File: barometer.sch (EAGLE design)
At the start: 91 parts, among them IC1 MIC5225-3.3v, IC2 TPS5410, IC3 ZPA2326-0311A-R, U1 MCP4725, U2 LTC2850, U3 PCA9306, U4 MAX3221, U5 XC6215XC6215B182NR, U6 Tiny85-20-SMT, X2 1751264, X3 1751248

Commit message: Migrate to customised/forked libraries
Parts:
- SJ1, SJ10, SJ11, SJ12, SJ2, SJ3, SJ4, SJ5, SJ6, SJ7, SJ8, SJ9: device SparkFun-Retired:SOLDERJUMPERTRACE -> SparkFun-Retired-0:SOLDERJUMPERTRACE
- U3: device SparkFun-IC-Comms:PCA9306 -> v-shifter-sparkfun:PCA9306
- U6: device SparkFun-Retired:ATTINY45TINY85-20-SMT -> SparkFun-Retired-0:ATTINY45TINY85-20-SMT
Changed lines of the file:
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@@
 <part name="TP4" library="testpad" library_urn="urn:adsk.eagle:library:385" deviceset="PTR1" device="B1,27" package3d_urn="urn:adsk.eagle:package:27944/1"/>
 <part name="TP5" library="testpad" library_urn="urn:adsk.eagle:library:385" deviceset="PTR1" device="B1,27" package3d_urn="urn:adsk.eagle:package:27944/1"/>
-<part name="SJ1" library="SparkFun-Retired" deviceset="SOLDERJUMPER" device="TRACE"/>
-<part name="SJ2" library="SparkFun-Retired" deviceset="SOLDERJUMPER" device="TRACE"/>
-<part name="SJ3" library="SparkFun-Retired" deviceset="SOLDERJUMPER" device="TRACE"/>
-<part name="SJ4" library="SparkFun-Retired" deviceset="SOLDERJUMPER" device="TRACE"/>
+<part name="SJ1" library="SparkFun-Retired-0" deviceset="SOLDERJUMPER" device="TRACE"/>
+<part name="SJ2" library="SparkFun-Retired-0" deviceset="SOLDERJUMPER" device="TRACE"/>
+<part name="SJ3" library="SparkFun-Retired-0" deviceset="SOLDERJUMPER" device="TRACE"/>
+<part name="SJ4" library="SparkFun-Retired-0" deviceset="SOLDERJUMPER" device="TRACE"/>
 <part name="U$1" library="microbuilder" deviceset="MOUNTINGHOLE" device="2.5"/>
 <part name="U$2" library="microbuilder" deviceset="MOUNTINGHOLE" device="2.5"/>
@@
 <part name="TP13" library="testpad" library_urn="urn:adsk.eagle:library:385" deviceset="PTR1" device="B1,27" package3d_urn="urn:adsk.eagle:package:27944/1"/>
 <part name="TP14" library="testpad" library_urn="urn:adsk.eagle:library:385" deviceset="PTR1" device="B1,27" package3d_urn="urn:adsk.eagle:package:27944/1"/>
-<part name="U6" library="SparkFun-Retired" deviceset="ATTINY45" device="TINY85-20-SMT" value="Tiny85-20-SMT"/>
-<part name="SJ5" library="SparkFun-Retired" deviceset="SOLDERJUMPER" device="TRACE"/>
-<part name="SJ6" library="SparkFun-Retired" deviceset="SOLDERJUMPER" device="TRACE"/>
-<part name="SJ7" library="SparkFun-Retired" deviceset="SOLDERJUMPER" device="TRACE"/>
-<part name="SJ8" library="SparkFun-Retired" deviceset="SOLDERJUMPER" device="TRACE"/>
-<part name="SJ9" library="SparkFun-Retired" deviceset="SOLDERJUMPER" device="TRACE"/>
+<part name="U6" library="SparkFun-Retired-0" deviceset="ATTINY45" device="TINY85-20-SMT" value="Tiny85-20-SMT"/>
+<part name="SJ5" library="SparkFun-Retired-0" deviceset="SOLDERJUMPER" device="TRACE"/>
+<part name="SJ6" library="SparkFun-Retired-0" deviceset="SOLDERJUMPER" device="TRACE"/>
+<part name="SJ7" library="SparkFun-Retired-0" deviceset="SOLDERJUMPER" device="TRACE"/>
+<part name="SJ8" library="SparkFun-Retired-0" deviceset="SOLDERJUMPER" device="TRACE"/>
+<part name="SJ9" library="SparkFun-Retired-0" deviceset="SOLDERJUMPER" device="TRACE"/>
 <part name="U1" library="microbuilder" deviceset="DAC_MCP4725" device="" value="MCP4725"/>
 <part name="X3" library="con-phoenix-350" library_urn="urn:adsk.eagle:library:174" deviceset="1751248" device="" package3d_urn="urn:adsk.eagle:package:9395/1"/>
 <part name="X2" library="con-phoenix-350" library_urn="urn:adsk.eagle:library:174" deviceset="1751264" device="" package3d_urn="urn:adsk.eagle:package:9397/1"/>
-<part name="U3" library="SparkFun-IC-Comms" deviceset="PCA9306" device="" value="PCA9306"/>
-<part name="SJ10" library="SparkFun-Retired" deviceset="SOLDERJUMPER" device="TRACE"/>
-<part name="SJ11" library="SparkFun-Retired" deviceset="SOLDERJUMPER" device="TRACE"/>
+<part name="U3" library="v-shifter-sparkfun" deviceset="PCA9306" device="" value="PCA9306"/>
+<part name="SJ10" library="SparkFun-Retired-0" deviceset="SOLDERJUMPER" device="TRACE"/>
+<part name="SJ11" library="SparkFun-Retired-0" deviceset="SOLDERJUMPER" device="TRACE"/>
 <part name="TP15" library="testpad" library_urn="urn:adsk.eagle:library:385" deviceset="PTR1" device="B1,27" package3d_urn="urn:adsk.eagle:package:27944/1"/>
 <part name="TP16" library="testpad" library_urn="urn:adsk.eagle:library:385" deviceset="PTR1" device="B1,27" package3d_urn="urn:adsk.eagle:package:27944/1"/>
@@
 <part name="C15" library="microbuilder" deviceset="CAP_CERAMIC" device="1206" value="47u"/>
 <part name="TP17" library="testpad" library_urn="urn:adsk.eagle:library:385" deviceset="PTR1" device="B1,27" package3d_urn="urn:adsk.eagle:package:27944/1"/>
-<part name="SJ12" library="SparkFun-Retired" deviceset="SOLDERJUMPER" device="TRACE"/>
+<part name="SJ12" library="SparkFun-Retired-0" deviceset="SOLDERJUMPER" device="TRACE"/>
 <part name="JP1" library="microbuilder" deviceset="HEADER-1X3" device="SMT" value="Analog Output Format"/>
 <part name="JP2" library="microbuilder" deviceset="HEADER-1X3" device="SMT" value="Digital Output Format"/>

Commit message: Update all libraries
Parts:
- D2: value B340A -> 3A/40V/500mV
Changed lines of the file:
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@@
 </classes>
 <parts>
-<part name="IC1" library="adafruit" deviceset="LP298X" device="S" value="MIC5225-3.3v"/>
-<part name="D1" library="adafruit" deviceset="DIODE" device="_SOD-123FL" value="SCHOTTKY"/>
+<part name="IC1" library="adafruit" library_urn="urn:adsk.eagle:library:420" deviceset="LP298X" device="S" value="MIC5225-3.3v"/>
+<part name="D1" library="adafruit" library_urn="urn:adsk.eagle:library:420" deviceset="DIODE" device="_SOD-123FL" value="SCHOTTKY"/>
 <part name="U4" library="texas-msp" deviceset="MAX3221" device="-TSSOP16" value="MAX3221"/>
 <part name="FRAME4" library="microbuilder" deviceset="FRAME_A4" device=""/>
@@
 <part name="C8" library="microbuilder" deviceset="CAP_CERAMIC" device="0603" value="4.7u"/>
 <part name="C9" library="microbuilder" deviceset="CAP_CERAMIC" device="0603" value="0.01u"/>
-<part name="D2" library="SparkFun-DiscreteSemi" deviceset="DIODE-SCHOTTKY" device="-B340A" value="B340A"/>
+<part name="D2" library="SparkFun-DiscreteSemi" library_urn="urn:adsk.eagle:library:514" deviceset="DIODE-SCHOTTKY" device="-B340A" package3d_urn="urn:adsk.eagle:package:38443/1" value="3A/40V/500mV"/>
 <part name="L1" library="Particle" deviceset="INDUCTOR-SPARKFUN" device="1210" value="68u"/>
 <part name="R20" library="microbuilder" deviceset="RESISTOR" device="0603" value="10k"/>

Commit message: Fix inductor's footprint's dimensions
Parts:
- L1: device Particle:INDUCTOR-SPARKFUN1210 -> inductor-tdk:INDUCTOR-TDKVLS6045EX
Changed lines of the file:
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@@
 <part name="C9" library="microbuilder" deviceset="CAP_CERAMIC" device="0603" value="0.01u"/>
 <part name="D2" library="SparkFun-DiscreteSemi" library_urn="urn:adsk.eagle:library:514" deviceset="DIODE-SCHOTTKY" device="-B340A" package3d_urn="urn:adsk.eagle:package:38443/1" value="3A/40V/500mV"/>
-<part name="L1" library="Particle" deviceset="INDUCTOR-SPARKFUN" device="1210" value="68u"/>
+<part name="L1" library="inductor-tdk" deviceset="INDUCTOR-TDK" device="VLS6045EX" value="68u"/>
 <part name="R20" library="microbuilder" deviceset="RESISTOR" device="0603" value="10k"/>
 <part name="R21" library="microbuilder" deviceset="RESISTOR" device="0603" value="3.24k"/>

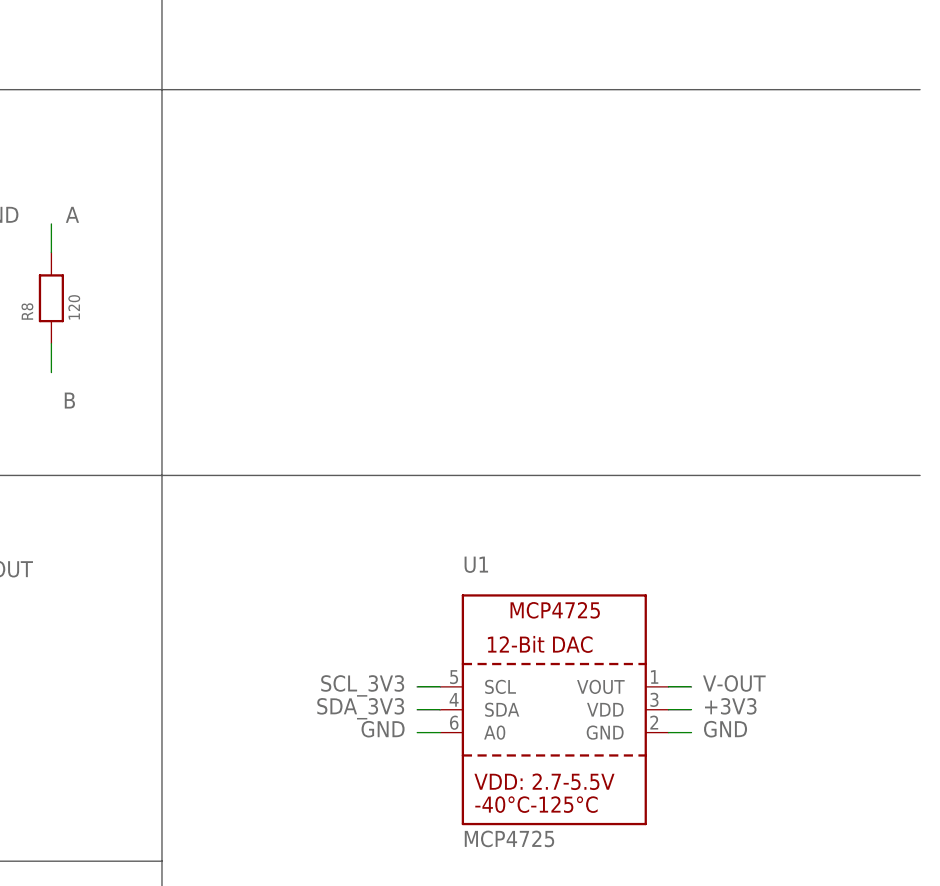
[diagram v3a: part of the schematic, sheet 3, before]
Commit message: Fix DAC output's voltage reference from +3V3 to +5V0
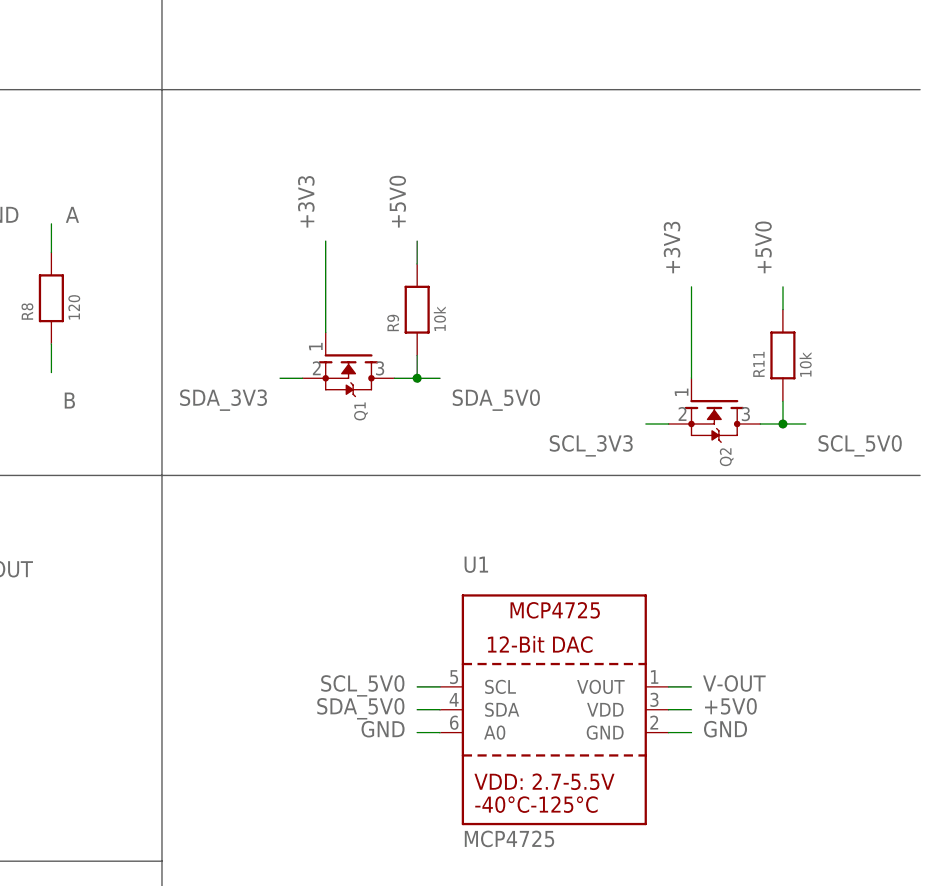
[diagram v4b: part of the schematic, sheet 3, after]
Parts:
- added Q1, Q2: (no value), microbuilder:MOSFET-NWIDE
- added R11, R9: 10k, microbuilder:RESISTOR0603
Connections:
- new net SCL_5V0: Q2.D, R11.1, U1.SCL
- new net SDA_5V0: Q1.D, R9.1, U1.SDA
- net +3V3: now also Q1.G, Q2.G; no longer U1.VDD
- net +5V0: now also R11.2, R9.2, U1.VDD
- net SCL_3V3: now also Q2.S; no longer U1.SCL
- net SDA_3V3: now also Q1.S; no longer U1.SDA
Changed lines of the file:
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@@
 <classes>
 <class number="0" name="default" width="0" drill="0">
-<clearance class="0" value="0.205"/>
 </class>
 <class number="1" name="power" width="0.3048" drill="0">
@@
 <part name="PAD2" library="wirepad" library_urn="urn:adsk.eagle:library:412" deviceset="SMD2" device="" package3d_urn="urn:adsk.eagle:package:30839/1"/>
 <part name="PAD3" library="wirepad" library_urn="urn:adsk.eagle:library:412" deviceset="SMD2" device="" package3d_urn="urn:adsk.eagle:package:30839/1"/>
+<part name="R9" library="microbuilder" deviceset="RESISTOR" device="0603" value="10k"/>
+<part name="R11" library="microbuilder" deviceset="RESISTOR" device="0603" value="10k"/>
+<part name="Q1" library="microbuilder" deviceset="MOSFET-N" device="WIDE"/>
+<part name="Q2" library="microbuilder" deviceset="MOSFET-N" device="WIDE"/>
 </parts>
 <sheets>
@@
 <instance part="JP1" gate="A" x="46.99" y="35.56"/>
 <instance part="JP2" gate="A" x="46.99" y="15.24"/>
+<instance part="R9" gate="G$1" x="200.66" y="107.95" rot="R90"/>
+<instance part="R11" gate="G$1" x="241.3" y="102.87" rot="R90"/>
+<instance part="Q1" gate="G$1" x="193.04" y="102.87" rot="R270"/>
+<instance part="Q2" gate="G$1" x="233.68" y="97.79" rot="R270"/>
 </instances>
 <busses>
@@
 </segment>
 <segment>
-<pinref part="U1" gate="G$1" pin="VDD"/>
-<wire x1="228.6" y1="63.5" x2="231.14" y2="63.5" width="0.1524" layer="91"/>
-<label x="232.41" y="64.77" size="1.778" layer="95" rot="MR180"/>
+<wire x1="190.5" y1="105.41" x2="190.5" y2="115.57" width="0.1524" layer="91"/>
+<pinref part="Q1" gate="G$1" pin="G"/>
+<label x="189.23" y="116.84" size="1.778" layer="95" font="vector" rot="R90"/>
+</segment>
+<segment>
+<wire x1="231.14" y1="100.33" x2="231.14" y2="110.49" width="0.1524" layer="91"/>
+<pinref part="Q2" gate="G$1" pin="G"/>
+<label x="229.87" y="111.76" size="1.778" layer="95" font="vector" rot="R90"/>
 </segment>
 </net>
@@
 <net name="SDA_3V3" class="0">
 <segment>
+<wire x1="187.96" y1="100.33" x2="185.42" y2="100.33" width="0.1524" layer="91"/>
+<label x="184.15" y="99.06" size="1.778" layer="95" font="vector" rot="R180"/>
+<pinref part="Q1" gate="G$1" pin="S"/>
+</segment>
+</net>
+<net name="SCL_3V3" class="0">
+<segment>
+<wire x1="228.6" y1="95.25" x2="226.06" y2="95.25" width="0.1524" layer="91"/>
+<label x="224.79" y="93.98" size="1.778" layer="95" font="vector" rot="R180"/>
+<pinref part="Q2" gate="G$1" pin="S"/>
+</segment>
+</net>
+<net name="A-OUT" class="0">
+<segment>
+<wire x1="123.19" y1="13.97" x2="125.73" y2="13.97" width="0.1524" layer="91"/>
+<label x="127" y="15.24" size="1.778" layer="95"/>
+<pinref part="X2" gate="-3" pin="K"/>
+</segment>
+<segment>
+<wire x1="44.45" y1="35.56" x2="38.1" y2="35.56" width="0.1524" layer="91"/>
+<label x="36.83" y="36.83" size="1.778" layer="95" font="vector" rot="R180"/>
+<pinref part="JP1" gate="A" pin="2"/>
+</segment>
+</net>
+<net name="V-OUT" class="0">
+<segment>
+<pinref part="U1" gate="G$1" pin="VOUT"/>
+<wire x1="228.6" y1="66.04" x2="231.14" y2="66.04" width="0.1524" layer="91"/>
+<label x="232.41" y="67.31" size="1.778" layer="95" rot="MR180"/>
+</segment>
+<segment>
+<wire x1="44.45" y1="38.1" x2="38.1" y2="38.1" width="0.1524" layer="91"/>
+<label x="36.83" y="39.37" size="1.778" layer="95" font="vector" rot="R180"/>
+<pinref part="JP1" gate="A" pin="1"/>
+</segment>
+<segment>
+<pinref part="TP15" gate="G$1" pin="TP"/>
+<wire x1="50.8" y1="154.94" x2="50.8" y2="157.48" width="0.1524" layer="91"/>
+<label x="52.07" y="158.75" size="1.778" layer="95" rot="R90"/>
+</segment>
+</net>
+<net name="I-OUT" class="0">
+<segment>
+<wire x1="44.45" y1="33.02" x2="38.1" y2="33.02" width="0.1524" layer="91"/>
+<label x="36.83" y="34.29" size="1.778" layer="95" font="vector" rot="R180"/>
+<pinref part="JP1" gate="A" pin="3"/>
+</segment>
+<segment>
+<pinref part="TP16" gate="G$1" pin="TP"/>
+<wire x1="55.88" y1="154.94" x2="55.88" y2="157.48" width="0.1524" layer="91"/>
+<label x="57.15" y="158.75" size="1.778" layer="95" rot="R90"/>
+</segment>
+</net>
+<net name="SDA_5V0" class="0">
+<segment>
+<wire x1="198.12" y1="100.33" x2="200.66" y2="100.33" width="0.1524" layer="91"/>
+<wire x1="200.66" y1="100.33" x2="203.2" y2="100.33" width="0.1524" layer="91"/>
+<wire x1="200.66" y1="102.87" x2="200.66" y2="100.33" width="0.1524" layer="91"/>
+<junction x="200.66" y="100.33"/>
+<label x="204.47" y="99.06" size="1.778" layer="95" font="vector" align="top-left"/>
+<pinref part="R9" gate="G$1" pin="1"/>
+<pinref part="Q1" gate="G$1" pin="D"/>
+</segment>
+<segment>
 <pinref part="U1" gate="G$1" pin="SDA"/>
 <wire x1="203.2" y1="63.5" x2="200.66" y2="63.5" width="0.1524" layer="91"/>
@@
 </segment>
 </net>
-<net name="SCL_3V3" class="0">
+<net name="+5V0" class="0">
+<segment>
+<wire x1="200.66" y1="113.03" x2="200.66" y2="115.57" width="0.1524" layer="91"/>
+<pinref part="R9" gate="G$1" pin="2"/>
+<label x="199.39" y="116.84" size="1.778" layer="95" font="vector" rot="R90"/>
+</segment>
+<segment>
+<wire x1="241.3" y1="107.95" x2="241.3" y2="110.49" width="0.1524" layer="91"/>
+<pinref part="R11" gate="G$1" pin="2"/>
+<label x="240.03" y="111.76" size="1.778" layer="95" font="vector" rot="R90"/>
+</segment>
+<segment>
+<pinref part="U1" gate="G$1" pin="VDD"/>
+<wire x1="228.6" y1="63.5" x2="231.14" y2="63.5" width="0.1524" layer="91"/>
+<label x="232.41" y="64.77" size="1.778" layer="95" rot="MR180"/>
+</segment>
+</net>
+<net name="SCL_5V0" class="0">
+<segment>
+<wire x1="238.76" y1="95.25" x2="241.3" y2="95.25" width="0.1524" layer="91"/>
+<wire x1="241.3" y1="95.25" x2="243.84" y2="95.25" width="0.1524" layer="91"/>
+<wire x1="241.3" y1="97.79" x2="241.3" y2="95.25" width="0.1524" layer="91"/>
+<junction x="241.3" y="95.25"/>
+<label x="245.11" y="93.98" size="1.778" layer="95" font="vector" align="top-left"/>
+<pinref part="R11" gate="G$1" pin="1"/>
+<pinref part="Q2" gate="G$1" pin="D"/>
+</segment>
 <segment>
 <pinref part="U1" gate="G$1" pin="SCL"/>
@@
 </segment>
 </net>
-<net name="A-OUT" class="0">
-<segment>
-<wire x1="123.19" y1="13.97" x2="125.73" y2="13.97" width="0.1524" layer="91"/>
-<label x="127" y="15.24" size="1.778" layer="95"/>
-<pinref part="X2" gate="-3" pin="K"/>
-</segment>
-<segment>
-<wire x1="44.45" y1="35.56" x2="38.1" y2="35.56" width="0.1524" layer="91"/>
-<label x="36.83" y="36.83" size="1.778" layer="95" font="vector" rot="R180"/>
-<pinref part="JP1" gate="A" pin="2"/>
-</segment>
-</net>
-<net name="V-OUT" class="0">
-<segment>
-<pinref part="U1" gate="G$1" pin="VOUT"/>
-<wire x1="228.6" y1="66.04" x2="231.14" y2="66.04" width="0.1524" layer="91"/>
-<label x="232.41" y="67.31" size="1.778" layer="95" rot="MR180"/>
-</segment>
-<segment>
-<wire x1="44.45" y1="38.1" x2="38.1" y2="38.1" width="0.1524" layer="91"/>
-<label x="36.83" y="39.37" size="1.778" layer="95" font="vector" rot="R180"/>
-<pinref part="JP1" gate="A" pin="1"/>
-</segment>
-<segment>
-<pinref part="TP15" gate="G$1" pin="TP"/>
-<wire x1="50.8" y1="154.94" x2="50.8" y2="157.48" width="0.1524" layer="91"/>
-<label x="52.07" y="158.75" size="1.778" layer="95" rot="R90"/>
-</segment>
-</net>
-<net name="I-OUT" class="0">
-<segment>
-<wire x1="44.45" y1="33.02" x2="38.1" y2="33.02" width="0.1524" layer="91"/>
-<label x="36.83" y="34.29" size="1.778" layer="95" font="vector" rot="R180"/>
-<pinref part="JP1" gate="A" pin="3"/>
-</segment>
-<segment>
-<pinref part="TP16" gate="G$1" pin="TP"/>
-<wire x1="55.88" y1="154.94" x2="55.88" y2="157.48" width="0.1524" layer="91"/>
-<label x="57.15" y="158.75" size="1.778" layer="95" rot="R90"/>
-</segment>
-</net>

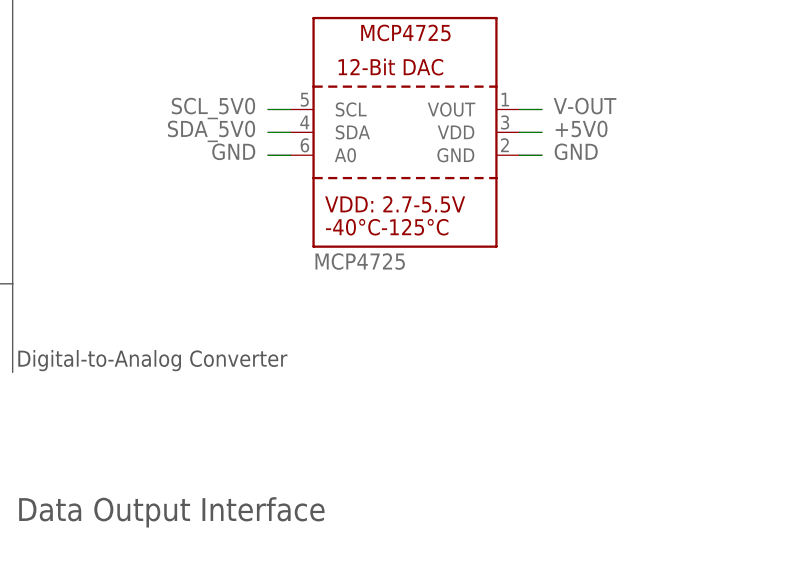
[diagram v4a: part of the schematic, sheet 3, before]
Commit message: Indicate the I2C slave address corresponding to the evaluated DAC
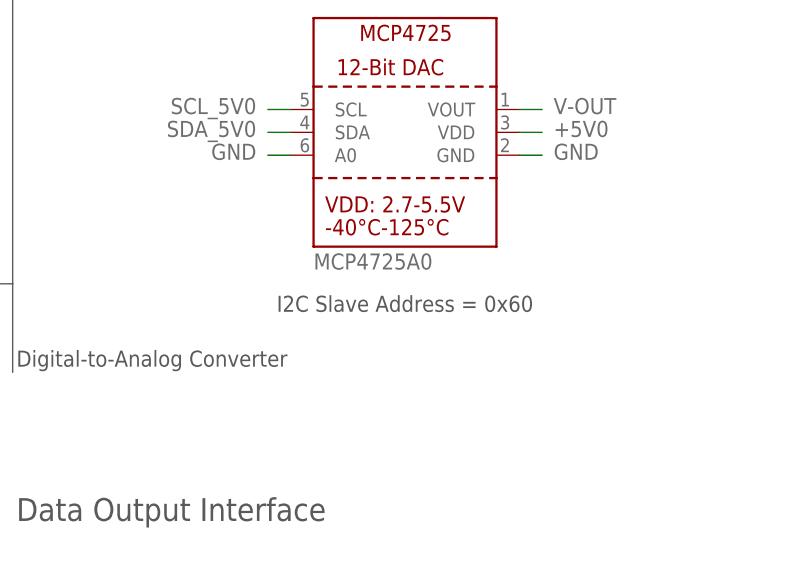
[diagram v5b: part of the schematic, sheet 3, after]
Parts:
- U1: value MCP4725 -> MCP4725A0
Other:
- note added: "I2C Slave Address = 0x60"
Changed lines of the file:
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@@
 <part name="SJ8" library="SparkFun-Retired-0" deviceset="SOLDERJUMPER" device="TRACE"/>
 <part name="SJ9" library="SparkFun-Retired-0" deviceset="SOLDERJUMPER" device="TRACE"/>
-<part name="U1" library="microbuilder" deviceset="DAC_MCP4725" device="" value="MCP4725"/>
+<part name="U1" library="microbuilder" deviceset="DAC_MCP4725" device="" value="MCP4725A0"/>
 <part name="X3" library="con-phoenix-350" library_urn="urn:adsk.eagle:library:174" deviceset="1751248" device="" package3d_urn="urn:adsk.eagle:package:9395/1"/>
 <part name="X2" library="con-phoenix-350" library_urn="urn:adsk.eagle:library:174" deviceset="1751264" device="" package3d_urn="urn:adsk.eagle:package:9397/1"/>
@@
 <text x="168.91" y="5.08" size="1.778" layer="97" font="vector" align="bottom-right">Degson Electrical
 15EDGRC-3.5-04P-14-00A-H</text>
+<text x="215.9" y="44.45" size="1.778" layer="97" font="vector" align="center">I2C Slave Address = 0x60</text>
 </plain>
 <instances>
